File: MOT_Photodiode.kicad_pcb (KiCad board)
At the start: 2 copper layers, 32 x 25 mm, 16 parts, among them J1 Supply, J2 output, J3 photodiode, U1 LT3032-12, U2 ADA4898-1YRDZ

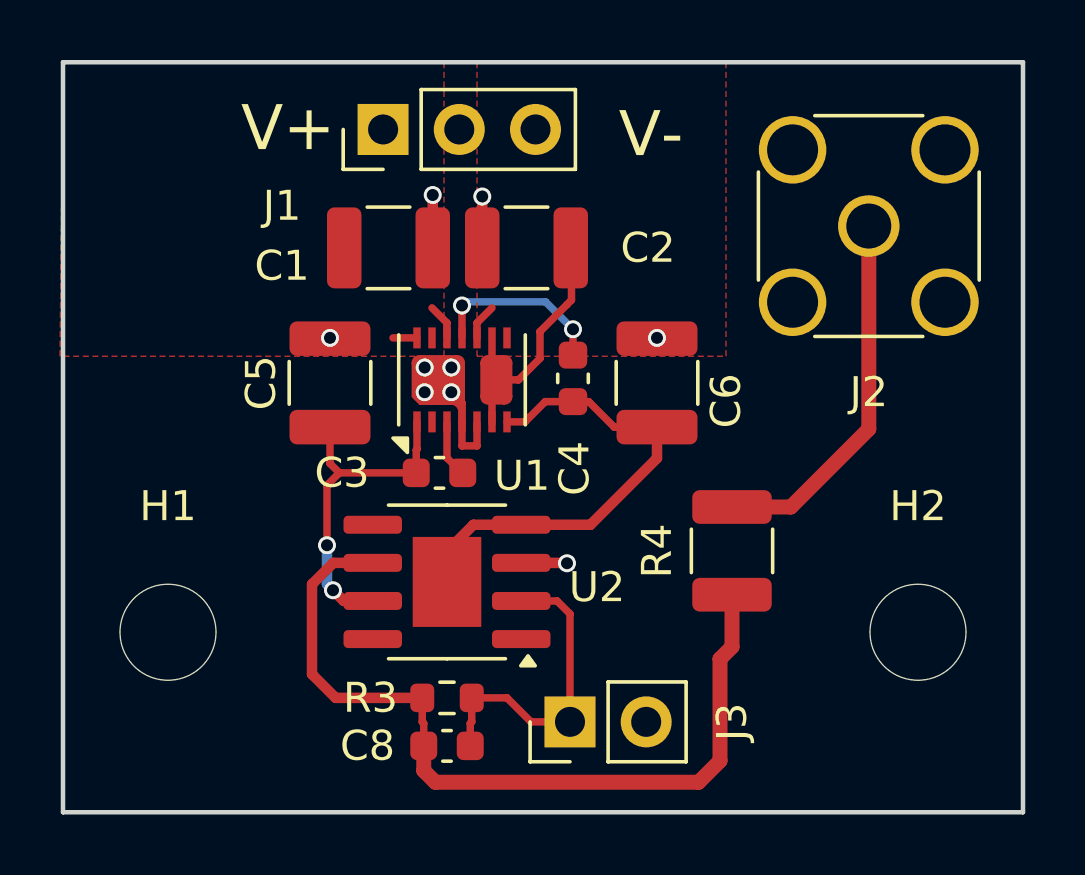
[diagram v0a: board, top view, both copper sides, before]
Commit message: Added logos
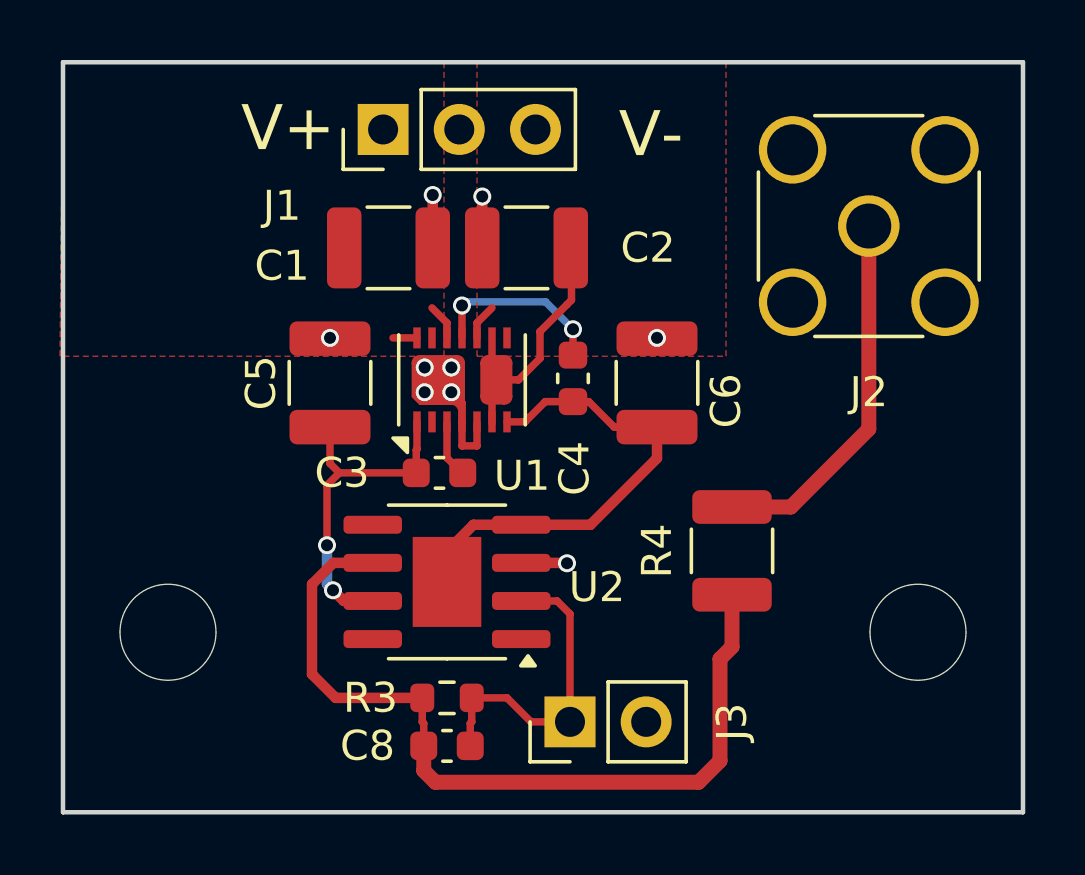
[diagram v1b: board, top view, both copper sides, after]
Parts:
- added SYM1: Logo_Open_Hardware_Small, Symbol:OSHW-Logo_7.5x8mm_SilkScreen, B.Cu at (148.2, 102.8)
- added SYM2: Logo_APQ, custom_footprints_project:APQ-Logo_small, B.Cu at (143.8, 100.8)
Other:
- board text added: "MOT_photodiode 1.1.0 Design: T. Preuschoff Date: 2025-02 https://github.com/ TU-Darmstadt-APQ"
- board text removed: "MOT_photodiode 02/2019 Rev 1.0"
